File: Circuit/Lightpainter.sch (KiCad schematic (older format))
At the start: 10 parts, among them K1 CONN_3, SW1 SW_PUSH, SW2 SW_PUSH, U1 78L05, U2 Arduino_Nano_v3, U3 SD_Card_Socket

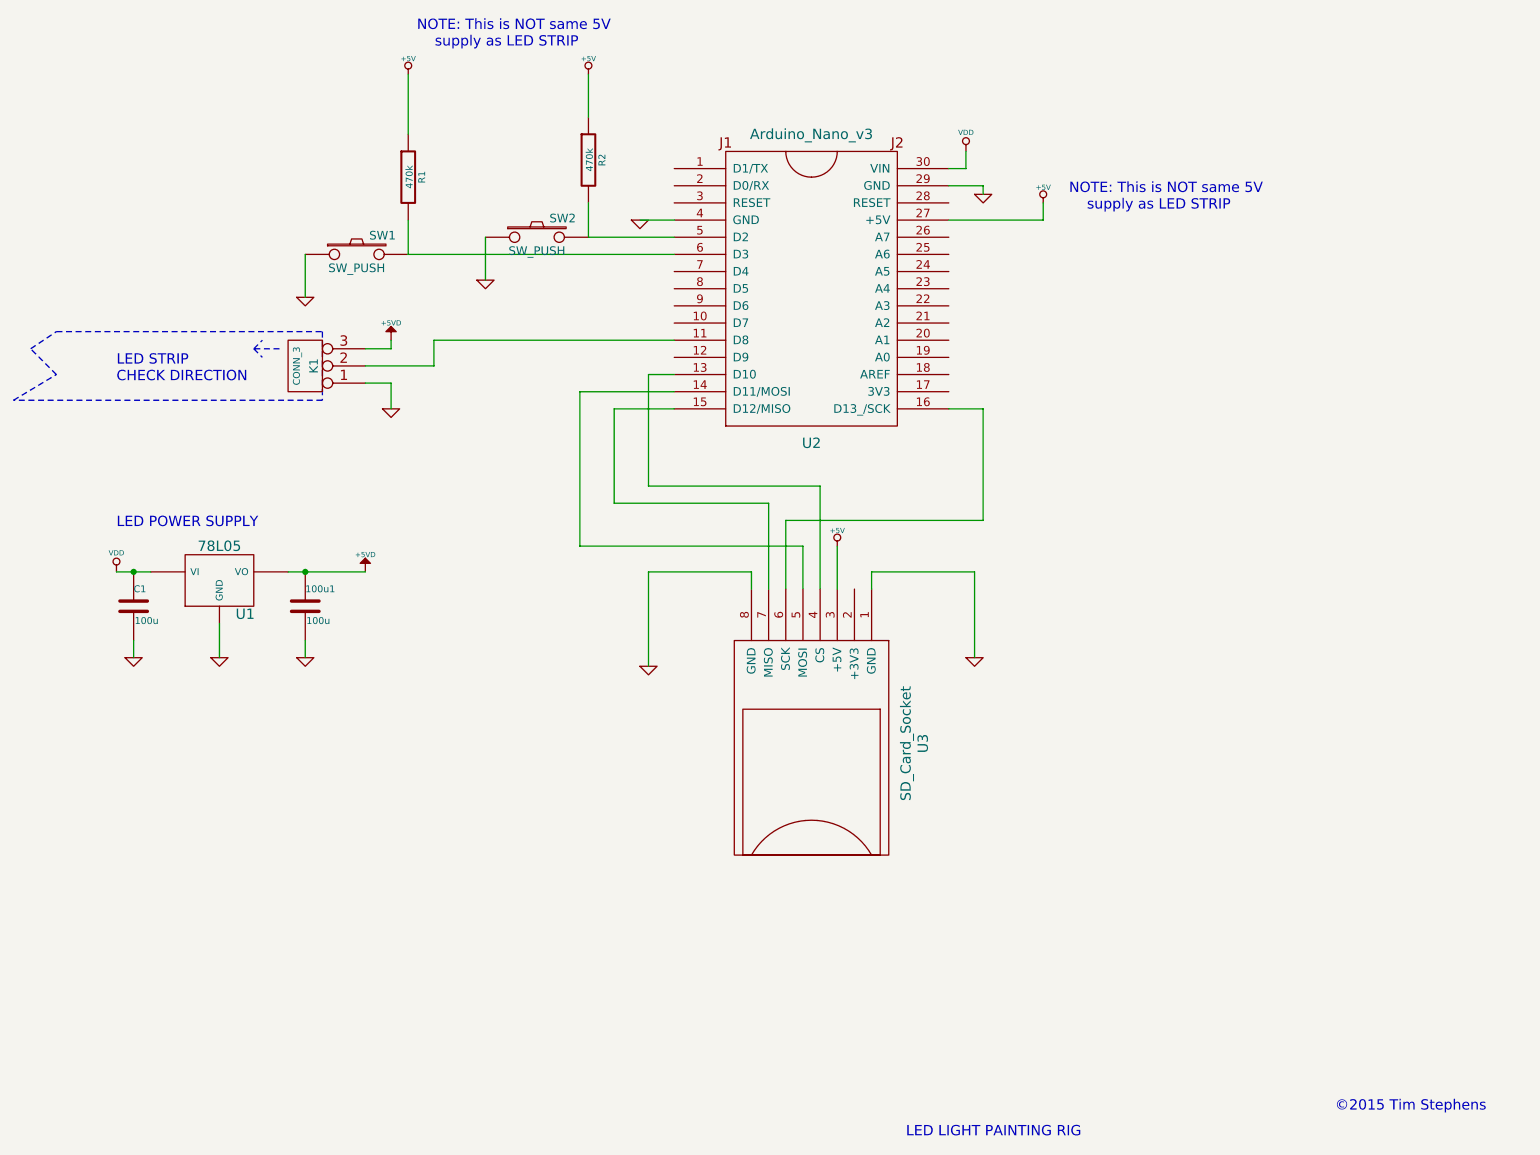
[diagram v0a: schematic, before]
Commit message: Change pin connections to match the Arduino code
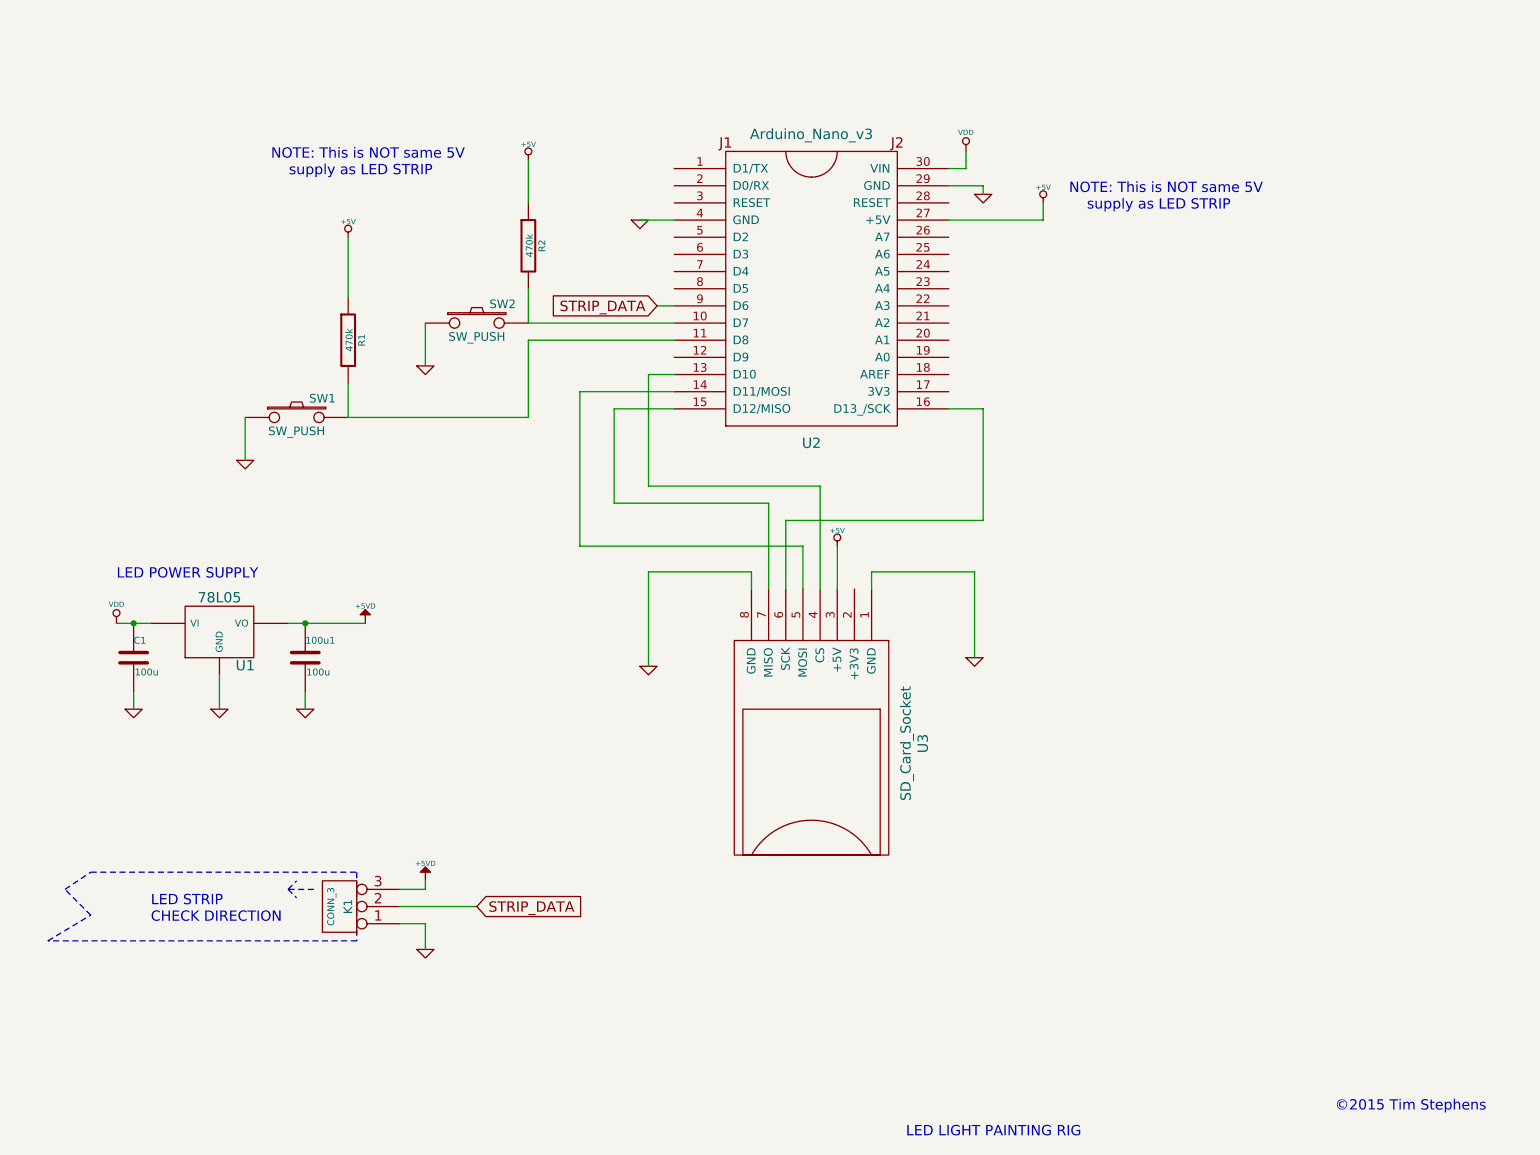
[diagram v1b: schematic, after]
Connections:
- net at U2.10 (D7): now also R2.2, SW2.2
- net at U2.11 (D8): now also R1.2, SW1.2; no longer K1.2 (PM)
- net STRIP_DATA: now reaches U2.9 (D6)
- net STRIP_DATA: now also K1.2 (PM)
- now unconnected: U2.5 (D2), U2.6 (D3)
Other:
- moved on the sheet: 100u1, C1, K1, R1, R2, SW1, SW2, U1

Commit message: Rats nest created
something has messed up the schematic, and the 7805 isn’t connected
properly. Rather than mess around to try to figure out the cause, edit
the .net file manually
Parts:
- renumbered 100u1 to C2
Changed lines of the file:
@@
 $EndDescr
-$Comp
-L 78L05 U1
-U 1 1 55244B5D
-P 3500 4550
-F 0 "U1" H 3650 4354 60  0000 C CNN
-F 1 "78L05" H 3500 4750 60  0000 C CNN
-F 2 "" H 3500 4550 60  0000 C CNN
-F 3 "" H 3500 4550 60  0000 C CNN
-	1    3500 4550
-	1    0    0    -1
-$EndComp
 $Comp
 L Arduino_Nano_v3 U2
@@
 $EndComp
 $Comp
-L C 100u1
+L C C2
 U 1 1 55244C15
 P 4000 4700
-F 0 "100u1" H 4000 4800 40  0000 L CNN
+F 0 "C2" H 4000 4800 40  0000 L CNN
 F 1 "100u" H 4006 4615 40  0000 L CNN
 F 2 "" H 4038 4550 30  0000 C CNN
@@
 $EndComp
 $Comp
-L GND #PWR2
+L GND #PWR01
 U 1 1 55244C36
 P 3000 5000
-F 0 "#PWR2" H 3000 5000 30  0001 C CNN
+F 0 "#PWR01" H 3000 5000 30  0001 C CNN
 F 1 "GND" H 3000 4930 30  0001 C CNN
 F 2 "" H 3000 5000 60  0000 C CNN
@@
 $EndComp
 $Comp
-L GND #PWR5
+L GND #PWR02
 U 1 1 55244C48
 P 4000 5000
-F 0 "#PWR5" H 4000 5000 30  0001 C CNN
+F 0 "#PWR02" H 4000 5000 30  0001 C CNN
 F 1 "GND" H 4000 4930 30  0001 C CNN
 F 2 "" H 4000 5000 60  0000 C CNN
@@
 $EndComp
 $Comp
-L GND #PWR10
+L GND #PWR03
 U 1 1 55244C53
 P 4700 3000
-F 0 "#PWR10" H 4700 3000 30  0001 C CNN
+F 0 "#PWR03" H 4700 3000 30  0001 C CNN
 F 1 "GND" H 4700 2930 30  0001 C CNN
 F 2 "" H 4700 3000 60  0000 C CNN
@@
 $EndComp
 $Comp
-L VDD #PWR1
+L VDD #PWR04
 U 1 1 55244C60
 P 2900 4500
-F 0 "#PWR1" H 2900 4600 30  0001 C CNN
+F 0 "#PWR04" H 2900 4600 30  0001 C CNN
 F 1 "VDD" H 2900 4610 30  0000 C CNN
 F 2 "" H 2900 4500 60  0000 C CNN
@@
 $EndComp
 Wire Wire Line
-	2900 4500 3100 4500
-Connection ~ 3000 4500
-Wire Wire Line
 	3000 4900 3000 5000
 Wire Wire Line
 	4000 4900 4000 5000
-Wire Wire Line
-	3900 4500 4350 4500
-$Comp
-L GND #PWR3
+$Comp
+L GND #PWR05
 U 1 1 55244C8E
 P 3500 5000
-F 0 "#PWR3" H 3500 5000 30  0001 C CNN
+F 0 "#PWR05" H 3500 5000 30  0001 C CNN
 F 1 "GND" H 3500 4930 30  0001 C CNN
 F 2 "" H 3500 5000 60  0000 C CNN
@@
 	1    0    0    -1
 $EndComp
-Wire Wire Line
-	3500 4800 3500 5000
-$Comp
-L +5VD #PWR6
+$Comp
+L +5VD #PWR06
 U 1 1 55244CA2
 P 4350 4500
-F 0 "#PWR6" H 4350 4450 20  0001 C CNN
+F 0 "#PWR06" H 4350 4450 20  0001 C CNN
 F 1 "+5VD" H 4350 4600 30  0000 C CNN
 F 2 "" H 4350 4500 60  0000 C CNN
@@
 	1    0    0    -1
 $EndComp
-Connection ~ 4000 4500
 Wire Wire Line
 	4250 3300 4250 3100
@@
 	4700 3000 4700 2750
 $Comp
-L GND #PWR4
+L GND #PWR07
 U 1 1 55244D89
 P 3650 3550
-F 0 "#PWR4" H 3650 3550 30  0001 C CNN
+F 0 "#PWR07" H 3650 3550 30  0001 C CNN
 F 1 "GND" H 3650 3480 30  0001 C CNN
 F 2 "" H 3650 3550 60  0000 C CNN
@@
 	5300 1800 5300 2050
 $Comp
-L VDD #PWR15
+L VDD #PWR08
 U 1 1 55245022
 P 7850 1750
-F 0 "#PWR15" H 7850 1850 30  0001 C CNN
+F 0 "#PWR08" H 7850 1850 30  0001 C CNN
 F 1 "VDD" H 7850 1860 30  0000 C CNN
 F 2 "" H 7850 1750 60  0000 C CNN
@@
 	7850 1850 7850 1750
 $Comp
-L GND #PWR17
+L GND #PWR09
 U 1 1 55245045
 P 7950 2000
-F 0 "#PWR17" H 7950 2000 30  0001 C CNN
+F 0 "#PWR09" H 7950 2000 30  0001 C CNN
 F 1 "GND" H 7950 1930 30  0001 C CNN
 F 2 "" H 7950 2000 60  0000 C CNN
@@
 	7950 1950 7950 2000
 $Comp
-L GND #PWR12
+L GND #PWR010
 U 1 1 5524506A
 P 5950 2150
-F 0 "#PWR12" H 5950 2150 30  0001 C CNN
+F 0 "#PWR010" H 5950 2150 30  0001 C CNN
 F 1 "GND" H 5950 2080 30  0001 C CNN
 F 2 "" H 5950 2150 60  0000 C CNN
@@
 	6150 2150 5950 2150
 $Comp
-L GND #PWR13
+L GND #PWR011
 U 1 1 552450A0
 P 6000 4750
-F 0 "#PWR13" H 6000 4750 30  0001 C CNN
+F 0 "#PWR011" H 6000 4750 30  0001 C CNN
 F 1 "GND" H 6000 4680 30  0001 C CNN
 F 2 "" H 6000 4750 60  0000 C CNN
@@
 	6000 4200 6000 4750
 $Comp
-L GND #PWR16
+L GND #PWR012
 U 1 1 55245188
 P 7900 4700
-F 0 "#PWR16" H 7900 4700 30  0001 C CNN
+F 0 "#PWR012" H 7900 4700 30  0001 C CNN
 F 1 "GND" H 7900 4630 30  0001 C CNN
 F 2 "" H 7900 4700 60  0000 C CNN
@@
 	7900 4200 7900 4700
 $Comp
-L +5V #PWR9
+L +5V #PWR013
 U 1 1 552451C7
 P 4250 2250
-F 0 "#PWR9" H 4250 2340 20  0001 C CNN
+F 0 "#PWR013" H 4250 2340 20  0001 C CNN
 F 1 "+5V" H 4250 2340 30  0000 C CNN
 F 2 "" H 4250 2250 60  0000 C CNN
@@
 $EndComp
 $Comp
-L +5V #PWR11
+L +5V #PWR014
 U 1 1 552451D9
 P 5300 1800
-F 0 "#PWR11" H 5300 1890 20  0001 C CNN
+F 0 "#PWR014" H 5300 1890 20  0001 C CNN
 F 1 "+5V" H 5300 1890 30  0000 C CNN
 F 2 "" H 5300 1800 60  0000 C CNN
@@
 $EndComp
 $Comp
-L +5V #PWR14
+L +5V #PWR015
 U 1 1 552451E4
 P 7100 4050
-F 0 "#PWR14" H 7100 4140 20  0001 C CNN
+F 0 "#PWR015" H 7100 4140 20  0001 C CNN
 F 1 "+5V" H 7100 4140 30  0000 C CNN
 F 2 "" H 7100 4050 60  0000 C CNN
@@
 	7100 4300 7100 4050
 $Comp
-L +5V #PWR18
+L +5V #PWR016
 U 1 1 55245222
 P 8300 2050
-F 0 "#PWR18" H 8300 2140 20  0001 C CNN
+F 0 "#PWR016" H 8300 2140 20  0001 C CNN
 F 1 "+5V" H 8300 2140 30  0000 C CNN
 F 2 "" H 8300 2050 60  0000 C CNN
@@
 	8300 2150 8300 2050
 $Comp
-L +5VD #PWR7
+L +5VD #PWR017
 U 1 1 552452C2
 P 4700 6000
-F 0 "#PWR7" H 4700 5950 20  0001 C CNN
+F 0 "#PWR017" H 4700 5950 20  0001 C CNN
 F 1 "+5VD" H 4700 6100 30  0000 C CNN
 F 2 "" H 4700 6000 60  0000 C CNN
@@
 	4700 6050 4700 6000
 $Comp
-L GND #PWR8
+L GND #PWR018
 U 1 1 552452FF
 P 4700 6400
-F 0 "#PWR8" H 4700 6400 30  0001 C CNN
+F 0 "#PWR018" H 4700 6400 30  0001 C CNN
 F 1 "GND" H 4700 6330 30  0001 C CNN
 F 2 "" H 4700 6400 60  0000 C CNN
@@
 Wire Wire Line
 	5300 3300 4250 3300
+Wire Wire Line
+	2900 4500 3100 4500
+Connection ~ 3000 4500
+Wire Wire Line
+	3900 4500 4350 4500
+Connection ~ 4000 4500
+Wire Wire Line
+	3500 4800 3500 5000
+Connection ~ 3900 4500
+Connection ~ 3100 4500
+$Comp
+L 78L05 U1
+U 1 1 5525A5E4
+P 3500 4550
+F 0 "U1" H 3650 4354 60  0000 C CNN
+F 1 "78L05" H 3500 4750 60  0000 C CNN
+F 2 "" H 3500 4550 60  0000 C CNN
+F 3 "" H 3500 4550 60  0000 C CNN
+	1    3500 4550
+	1    0    0    -1
+$EndComp
 $EndSCHEMATC
